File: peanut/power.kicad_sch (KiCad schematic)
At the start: 17 parts, among them J3 Battery JST, J4 Arming, Q5 PMOS, U4 LM3671MF, U5 TPS2116DRL

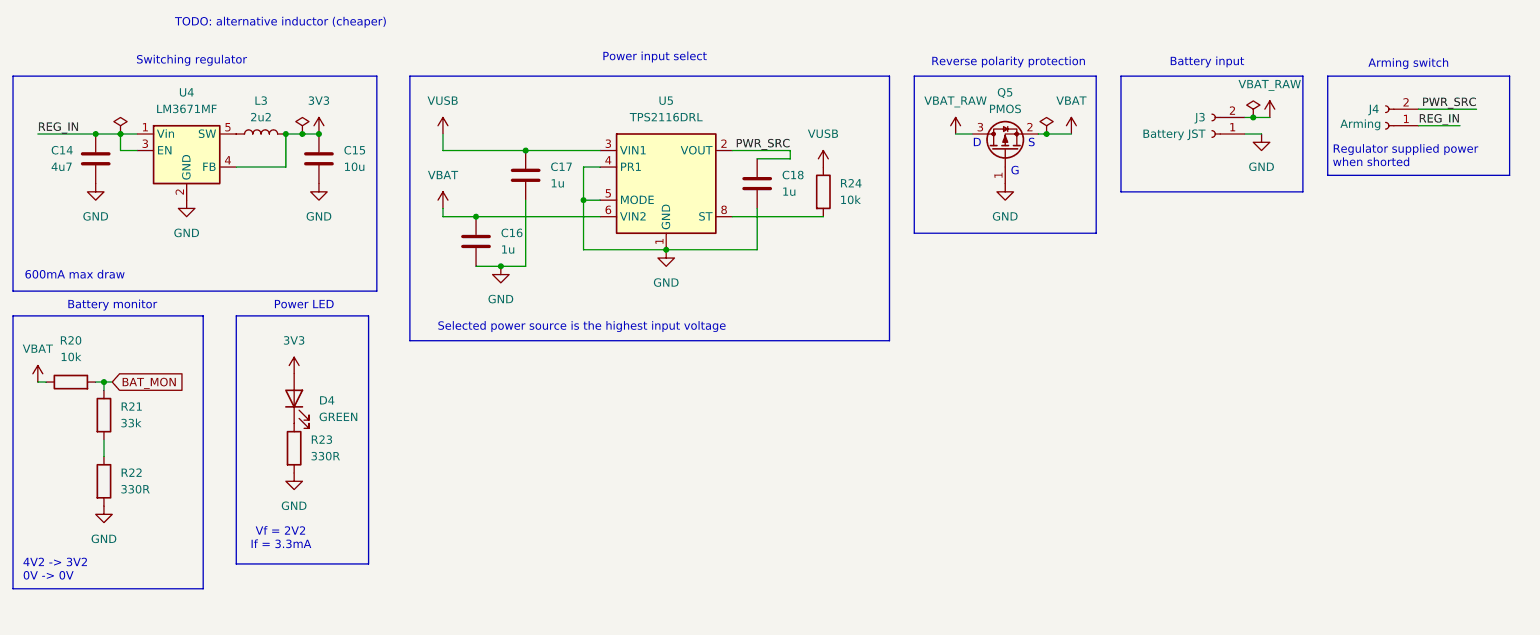
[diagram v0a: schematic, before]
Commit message: bug: Fix arming flaw
Fixed the arming circuitry so that the ARM terminal prevents power going
to the pyro channels. This means that the rest of the board can be
powered on before arming, which is good because:

- It allows configuring without arming
- Software arming can still be done as a second stage
- The MCU can be in low-power mode until told to arm over BLE
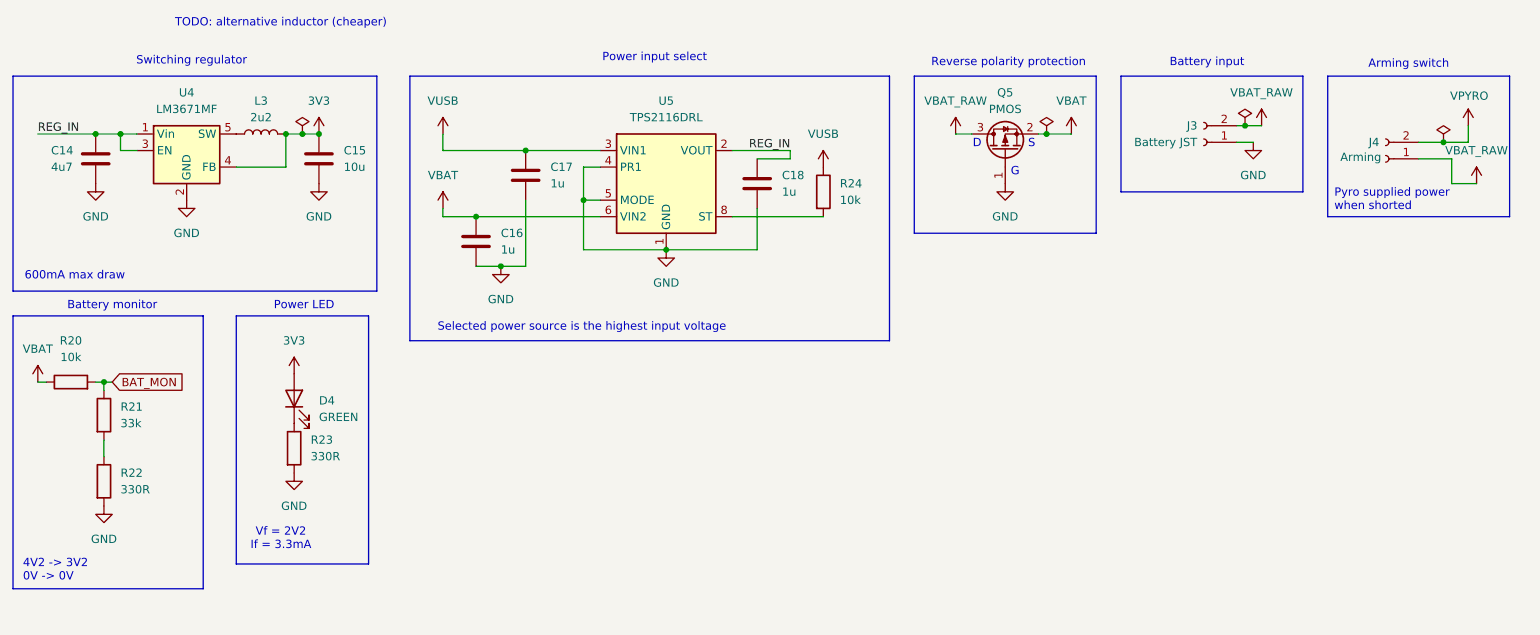
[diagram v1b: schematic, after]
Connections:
- net REG_IN: now also C18.1, U5.2 (VOUT), U5.7 (VOUT); no longer J4.1 (Pin_1)
- net VBAT_RAW: now also J4.1 (Pin_1)
- removed net PWR_SRC: C18.1, J4.2 (Pin_2), U5.2 (VOUT), U5.7 (VOUT)
- new net VPYRO: J4.2 (Pin_2)
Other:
- note added: "Pyro supplied power when shorted"
- note removed: "Regulator supplied power when shorted"
- moved on the sheet: J3, J4

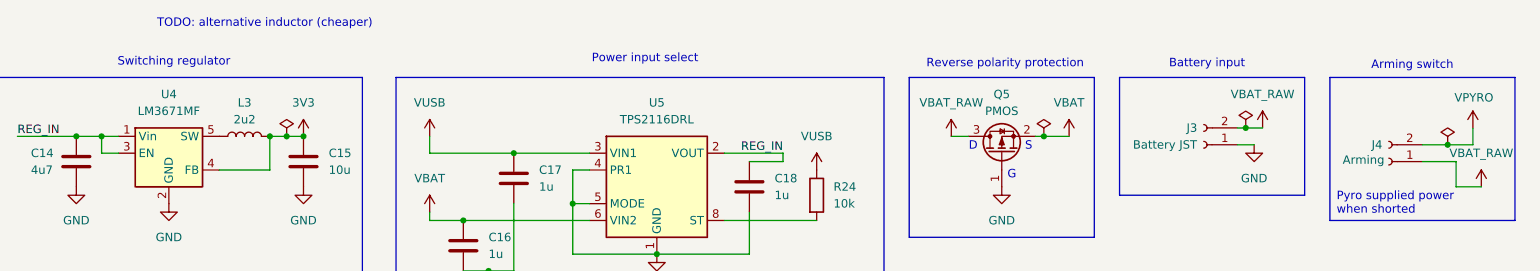
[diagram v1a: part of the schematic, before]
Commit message: feat: Better arming circuit
Improved the arming circuit connections so that both circuits are
powered off until armed.

Signed-off-by: Matteo Golin <matteo.golin@gmail.com>
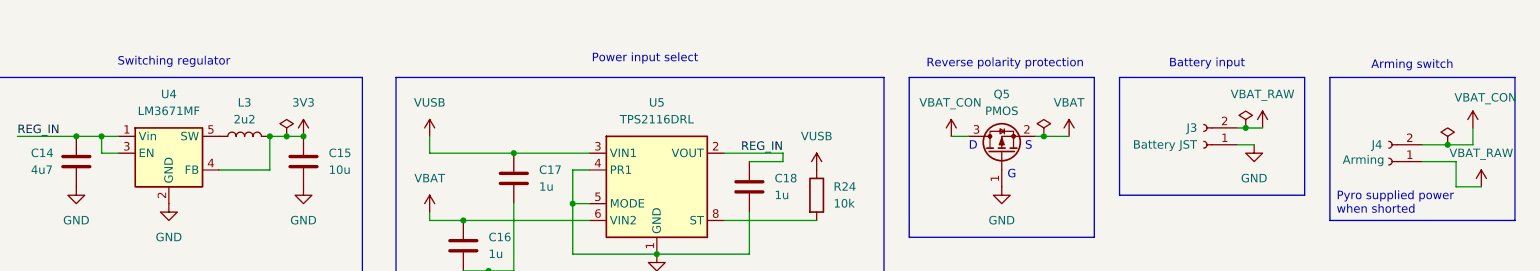
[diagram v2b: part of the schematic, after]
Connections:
- net VBAT_RAW: no longer Q5.3 (D)
- net VPYRO renamed VBAT_CON
- net VBAT_CON: now also Q5.3 (D)
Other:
- note removed: "TODO: alternative inductor (cheaper)"
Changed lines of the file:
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@@
-		)
-	)
-	(text "TODO: alternative inductor (cheaper)"
-		(exclude_from_sim no)
-		(at 80.518 51.562 0)
-		(effects
-			(font
-				(size 1.27 1.27)
-			)
 		)
 	)
@@
 			)
 		)
-		(property "Value" "VPYRO"
+		(property "Value" "VBAT_CON"
 			(at 260.096 62.738 0)
 			(show_name no)
@@
 		(in_pos_files yes)
 		(dnp no)
-		(fields_autoplaced yes)
 		(property "Reference" "#PWR037"
 			(at 184.15 72.39 0)
@@
 			)
 		)
-		(property "Value" "VBAT_RAW"
-			(at 184.15 63.5 0)
-			(show_name no)
-			(do_not_autoplace no)
-			(effects
-				(font
-					(size 1.27 1.27)
-				)
-			)
-		)
+		(property "Value" "VBAT_CON"
+			(at 179.324 63.5 0)
+			(show_name no)
+			(do_not_autoplace no)
+			(effects
+				(font
+					(size 1.27 1.27)
+				)
+				(justify left)
+			)
+		)

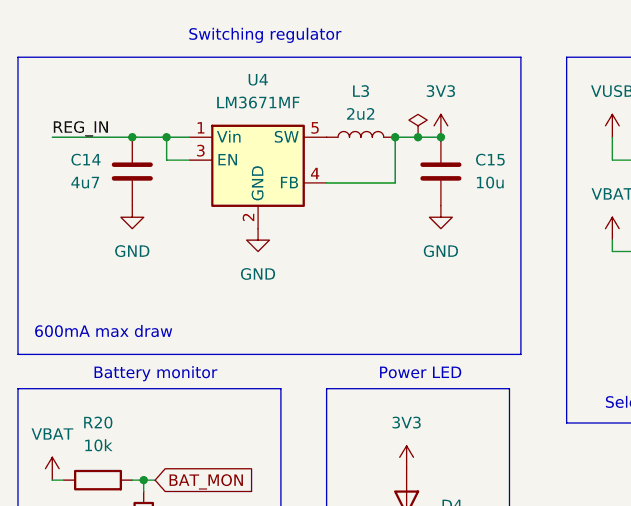
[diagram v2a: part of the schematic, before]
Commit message: chore: replace switching regulator with LDO
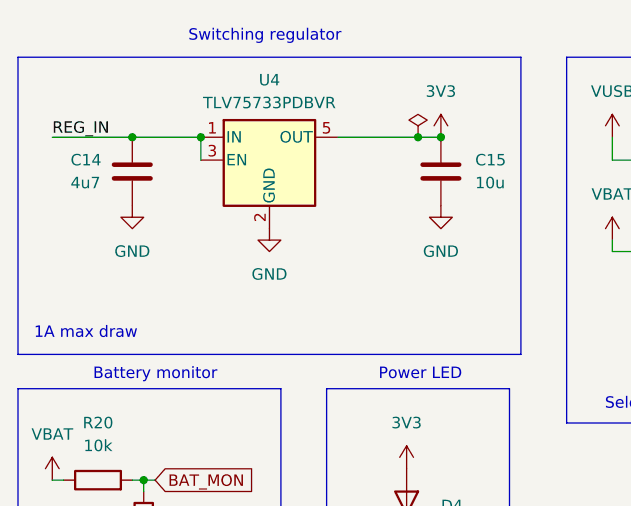
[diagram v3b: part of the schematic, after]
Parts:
- removed L3: 2u2, SRN3015BTA-2R2M:SRN3015BTA2R2M, symbol Device:L
- removed U4: LM3671MF, Package_TO_SOT_SMD:TSOT-23-5, symbol Regulator_Switching:LM3670MF
- added U4: TLV75733PDBVR, Package_TO_SOT_SMD:SOT-23-5, symbol Regulator_Linear:TLV75733PDBV
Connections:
- net 3V3: now also U4.5 (OUT)
- net GND: now also U4.2 (GND)
- net REG_IN: now also U4.1 (IN), U4.3 (EN)
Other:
- note added: "1A max draw"
- note removed: "600mA max draw"

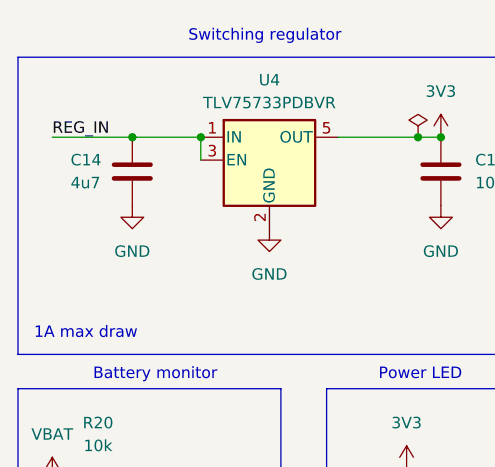
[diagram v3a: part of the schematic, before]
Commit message: chore: fix bulk capacitance value based on easymini selected value
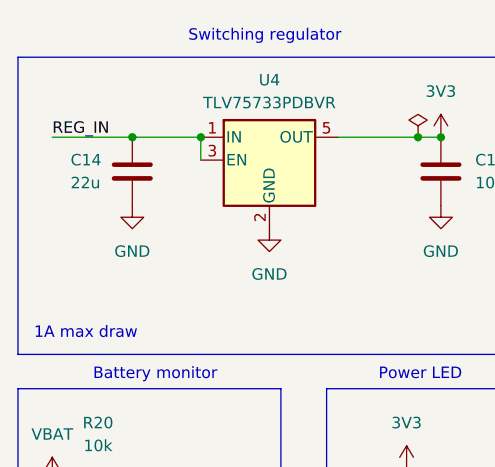
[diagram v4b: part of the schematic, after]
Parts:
- C14: value 4u7 -> 22u; MPN CGA3E1X5R0J475K080AC -> MLASJ168BB5226MTNA01
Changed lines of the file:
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@@
 			)
 		)
-		(property "Value" "4u7"
+		(property "Value" "22u"
 			(at 45.212 73.66 0)
 			(show_name no)
@@
 			)
 		)
-		(property "MPN" "CGA3E1X5R0J475K080AC"
+		(property "MPN" "MLASJ168BB5226MTNA01"
 			(at 52.07 72.39 0)
 			(hide yes)

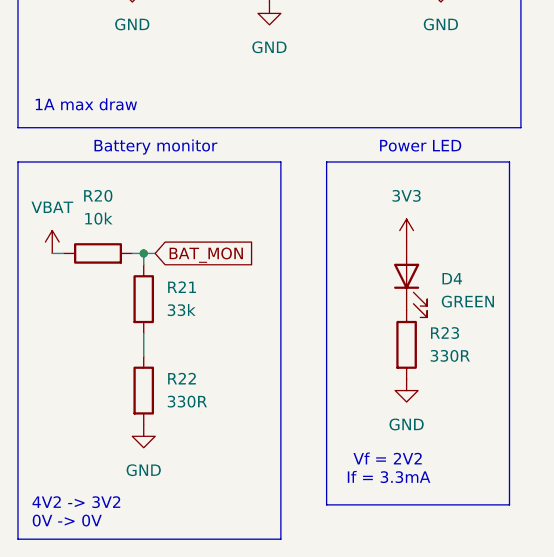
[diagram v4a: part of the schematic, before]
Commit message: Fix ADC voltage monitoring to use 1:1 ratio
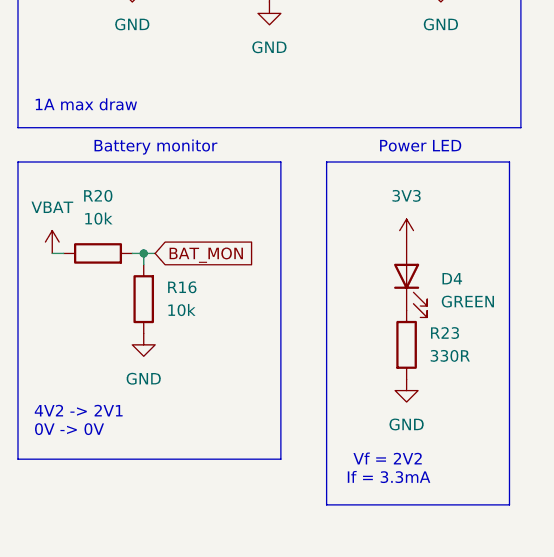
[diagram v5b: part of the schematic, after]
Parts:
- removed R21: 33k, Resistor_SMD:R_0402_1005Metric, symbol Device:R
- removed R22: 330R, Resistor_SMD:R_0402_1005Metric, symbol Device:R
- added R16: 10k, Resistor_SMD:R_0402_1005Metric, symbol Device:R
- U4: MPN (none) -> TLV75733PDBVR
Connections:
- net BAT_MON: now also R16.2
- net GND: now also R16.1
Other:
- note added: "4V2 -> 2V1 0V -> 0V"
- note removed: "4V2 -> 3V2 0V -> 0V"
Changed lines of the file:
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@@
 	(rectangle
 		(start 39.37 96.52)
-		(end 68.58 138.43)
+		(end 68.58 129.54)
 		(stroke
 			(width 0)
@@
 		)
 	)
-	(text "4V2 -> 3V2\n0V -> 0V"
+	(text "4V2 -> 2V1\n0V -> 0V"
 		(exclude_from_sim no)
-		(at 40.894 135.636 0)
+		(at 41.148 125.476 0)
 		(effects
 			(font
@@
 	(wire
 		(pts
-			(xy 53.34 115.57) (xy 53.34 118.11)
-		)
-		(stroke
-			(width 0)
-			(type default)
-		)
-	)
-	(wire
-		(pts
 			(xy 229.87 69.85) (xy 227.33 69.85)
 		)
@@
 	)
 	(symbol
-		(lib_id "Device:C")
-		(at 110.49 85.09 0)
+		(lib_id "Device:R")
+		(at 53.34 111.76 180)
 		(unit 1)
 		(body_style 1)
@@
 		(dnp no)
 		(fields_autoplaced yes)
-		(property "Reference" "C16"
-			(at 114.3 83.8199 0)
+		(property "Reference" "R16"
+			(at 55.88 110.4899 0)
 			(show_name no)
 			(do_not_autoplace no)
@@
 					(size 1.27 1.27)
 				)
-				(justify left)
+				(justify right)
 			)
 		)
-		(property "Value" "1u"
-			(at 114.3 86.3599 0)
+		(property "Value" "10k"
+			(at 55.88 113.0299 0)
 			(show_name no)
 			(do_not_autoplace no)
@@
 					(size 1.27 1.27)
 				)
-				(justify left)
+				(justify right)
 			)
 		)
-		(property "Footprint" "Capacitor_SMD:C_0603_1608Metric"
-			(at 111.4552 88.9 0)
+		(property "Footprint" "Resistor_SMD:R_0402_1005Metric"
+			(at 55.118 111.76 90)
 			(hide yes)
 			(show_name no)
@@
 		)
 		(property "Datasheet" ""
-			(at 110.49 85.09 0)
+			(at 53.34 111.76 0)
 			(hide yes)
 			(show_name no)
@@
 			)
 		)
-		(property "Description" "Unpolarized capacitor"
-			(at 110.49 85.09 0)
+		(property "Description" "Resistor"
+			(at 53.34 111.76 0)
 			(hide yes)
 			(show_name no)
@@
 			)
 		)
-		(property "MPN" "06036C105MAT2A"
-			(at 110.49 85.09 0)
+		(property "MPN" "MCS04020C1002FE000"
+			(at 53.34 111.76 90)
 			(hide yes)
 			(show_name no)
@@
 			(project "peanut"
 				(path "/5c6b6cfc-6c84-425a-9b66-e6111713aae8/f944ce75-1da7-4030-9ed2-502ac98b17ed"
-					(reference "C16")
+					(reference "R16")
 					(unit 1)
 				)
@@
 	)
 	(symbol
-		(lib_id "Device:R")
-		(at 53.34 121.92 0)
+		(lib_id "Device:C")
+		(at 110.49 85.09 0)
 		(unit 1)
 		(body_style 1)
@@
 		(dnp no)
 		(fields_autoplaced yes)
-		(property "Reference" "R22"
-			(at 55.88 120.6499 0)
+		(property "Reference" "C16"
+			(at 114.3 83.8199 0)
 			(show_name no)
 			(do_not_autoplace no)
@@
 			)
 		)
-		(property "Value" "330R"
-			(at 55.88 123.1899 0)
+		(property "Value" "1u"
+			(at 114.3 86.3599 0)
 			(show_name no)
 			(do_not_autoplace no)
@@
 			)
 		)
-		(property "Footprint" "Resistor_SMD:R_0402_1005Metric"
-			(at 51.562 121.92 90)
+		(property "Footprint" "Capacitor_SMD:C_0603_1608Metric"
+			(at 111.4552 88.9 0)
 			(hide yes)
 			(show_name no)
@@
 		)
 		(property "Datasheet" ""
-			(at 53.34 121.92 0)
+			(at 110.49 85.09 0)
 			(hide yes)
 			(show_name no)
@@
 			)
 		)
-		(property "Description" "Resistor"
-			(at 53.34 121.92 0)
+		(property "Description" "Unpolarized capacitor"
+			(at 110.49 85.09 0)
 			(hide yes)
 			(show_name no)
@@
 			)
 		)
-		(property "MPN" "560112110231"
-			(at 53.34 121.92 0)
+		(property "MPN" "06036C105MAT2A"
+			(at 110.49 85.09 0)
 			(hide yes)
 			(show_name no)
@@
 			(project "peanut"
 				(path "/5c6b6cfc-6c84-425a-9b66-e6111713aae8/f944ce75-1da7-4030-9ed2-502ac98b17ed"
-					(reference "R22")
+					(reference "C16")
 					(unit 1)
 				)
@@
 			)
 		)
+		(property "MPN" "TLV75733PDBVR"
+			(at 67.31 71.12 0)
+			(hide yes)
+			(show_name no)
+			(do_not_autoplace no)
+			(effects
+				(font
+					(size 1.27 1.27)
+				)
+			)
+		)
 		(pin "5"
 		)
@@
 	)
 	(symbol
-		(lib_id "Device:R")
-		(at 53.34 111.76 0)
-		(unit 1)
-		(body_style 1)
-		(exclude_from_sim no)
-		(in_bom yes)
-		(on_board yes)
-		(in_pos_files yes)
-		(dnp no)
-		(fields_autoplaced yes)
-		(property "Reference" "R21"
-			(at 55.88 110.4899 0)
-			(show_name no)
-			(do_not_autoplace no)
-			(effects
-				(font
-					(size 1.27 1.27)
-				)
-				(justify left)
-			)
-		)
-		(property "Value" "33k"
-			(at 55.88 113.0299 0)
-			(show_name no)
-			(do_not_autoplace no)
-			(effects
-				(font
-					(size 1.27 1.27)
-				)
-				(justify left)
-			)
-		)
-		(property "Footprint" "Resistor_SMD:R_0402_1005Metric"
-			(at 51.562 111.76 90)
-			(hide yes)
-			(show_name no)
-			(do_not_autoplace no)
-			(effects
-				(font
-					(size 1.27 1.27)
-				)
-			)
-		)
-		(property "Datasheet" ""
-			(at 53.34 111.76 0)
-			(hide yes)
-			(show_name no)
-			(do_not_autoplace no)
-			(effects
-				(font
-					(size 1.27 1.27)
-				)
-			)
-		)
-		(property "Description" "Resistor"
-			(at 53.34 111.76 0)
-			(hide yes)
-			(show_name no)
-			(do_not_autoplace no)
-			(effects
-				(font
-					(size 1.27 1.27)
-				)
-			)
-		)
-		(property "MPN" "MR04X3302FTL"
-			(at 53.34 111.76 0)
-			(hide yes)
-			(show_name no)
-			(do_not_autoplace no)
-			(effects
-				(font
-					(size 1.27 1.27)
-				)
-			)
-		)
-		(pin "2"
-		)
-		(pin "1"
-		)
-		(instances
-			(project "peanut"
-				(path "/5c6b6cfc-6c84-425a-9b66-e6111713aae8/f944ce75-1da7-4030-9ed2-502ac98b17ed"
-					(reference "R21")
-					(unit 1)
-				)
-			)
-		)
-	)
-	(symbol
 		(lib_id "power:GND")
-		(at 53.34 125.73 0)
+		(at 53.34 115.57 0)
 		(unit 1)
 		(body_style 1)
@@
 		(fields_autoplaced yes)
 		(property "Reference" "#PWR041"
-			(at 53.34 132.08 0)
+			(at 53.34 121.92 0)
 			(hide yes)
 			(show_name no)
@@
 		)
 		(property "Value" "GND"
-			(at 53.34 130.81 0)
+			(at 53.34 120.65 0)
 			(show_name no)
 			(do_not_autoplace no)
@@
 		)
 		(property "Footprint" ""
-			(at 53.34 125.73 0)
+			(at 53.34 115.57 0)
 			(hide yes)
 			(show_name no)
@@
 		)
 		(property "Datasheet" ""
-			(at 53.34 125.73 0)
+			(at 53.34 115.57 0)
 			(hide yes)
 			(show_name no)
@@
 		)
 		(property "Description" "Power symbol creates a global label with name \"GND\" , ground"
-			(at 53.34 125.73 0)
+			(at 53.34 115.57 0)
 			(hide yes)
 			(show_name no)

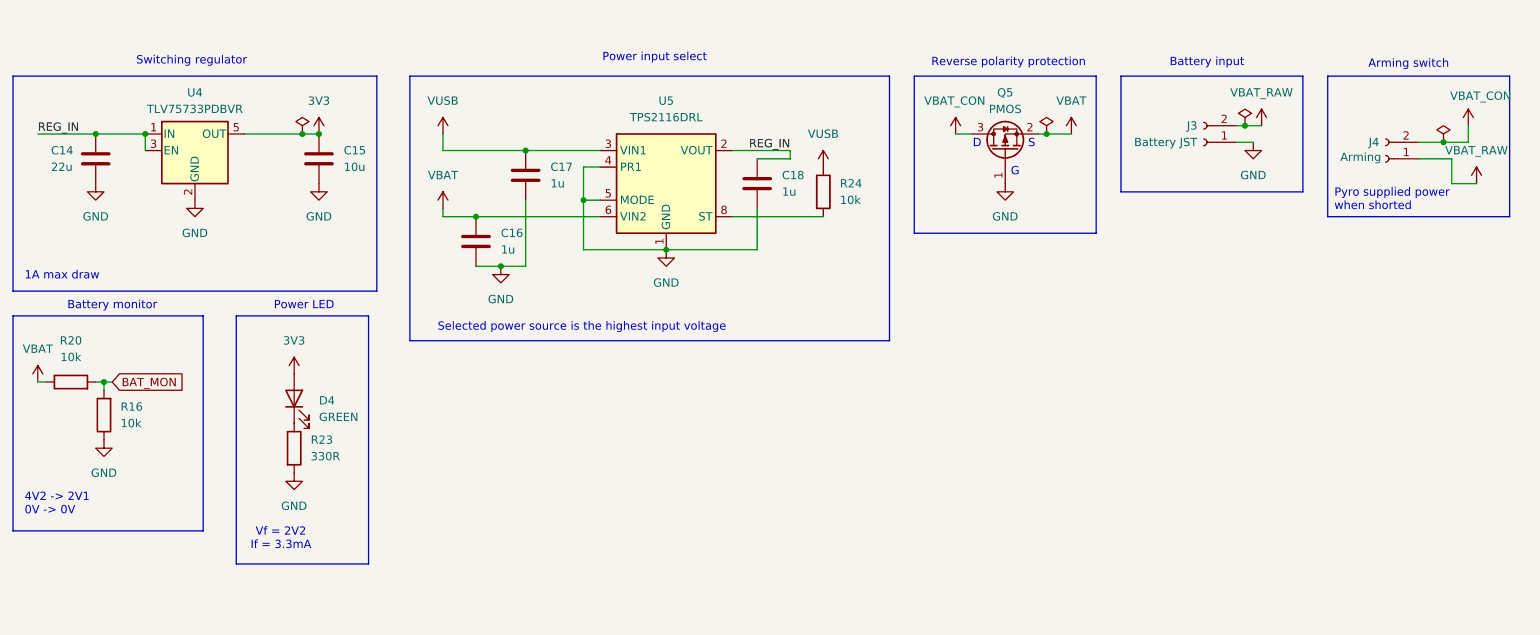
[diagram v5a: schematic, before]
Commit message: feat: improve reverse polarity protection circuit
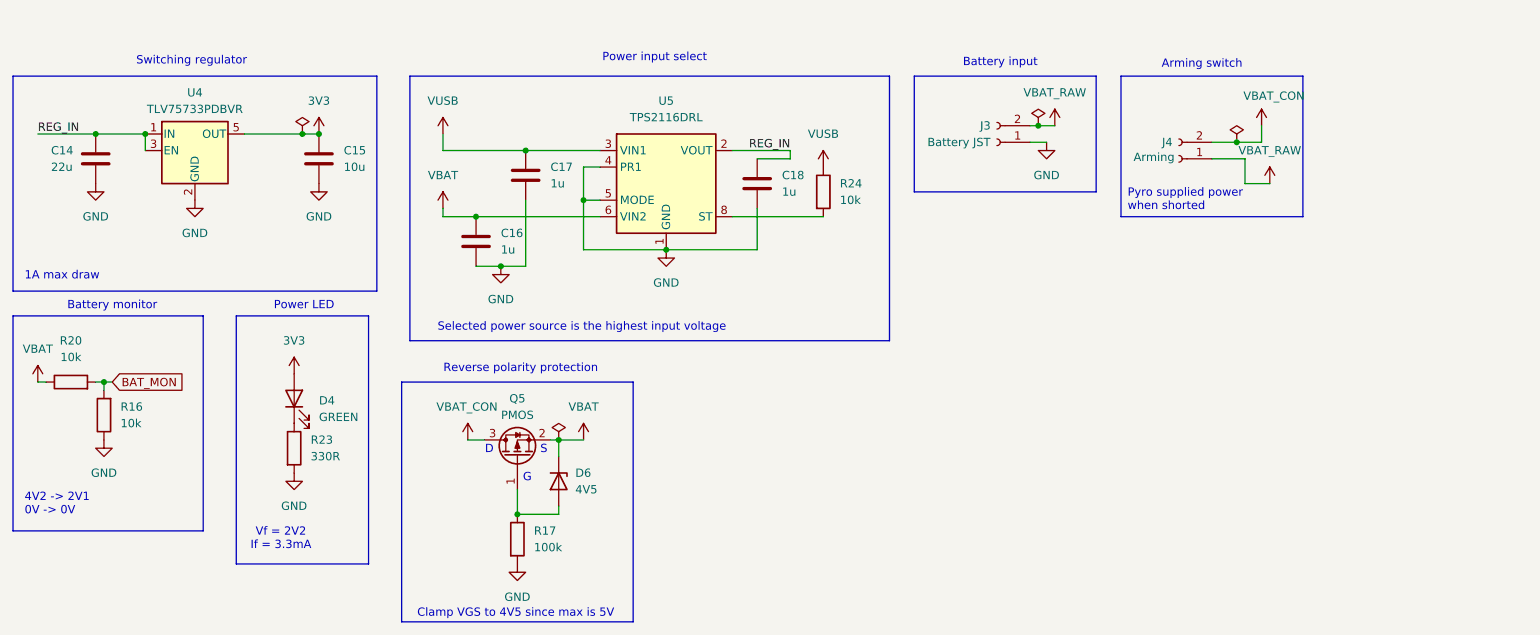
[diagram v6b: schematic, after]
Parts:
- added D6: 4V5, Diode_SMD:D_SOD-323, symbol Device:D_Zener
- added R17: 100k, Resistor_SMD:R_0402_1005Metric, symbol Device:R
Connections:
- net GND: now also R17.2; no longer Q5.1 (G)
- net VBAT: now also D6.1 (K)
- new net: D6.2 (A), Q5.1 (G), R17.1
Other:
- note added: "Clamp VGS to 4V5 since max is 5V"
- moved on the sheet: J3, J4, Q5
